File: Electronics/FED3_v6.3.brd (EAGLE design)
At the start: 108 x 50 mm, 50 parts, among them IC1 RTC_PCF8523T, IC2 TB6612 SSOP, IC3 M74VHC1GT50DTT1G, Q1 32.768, Q2 DMG3415, SW1 SSSS811101

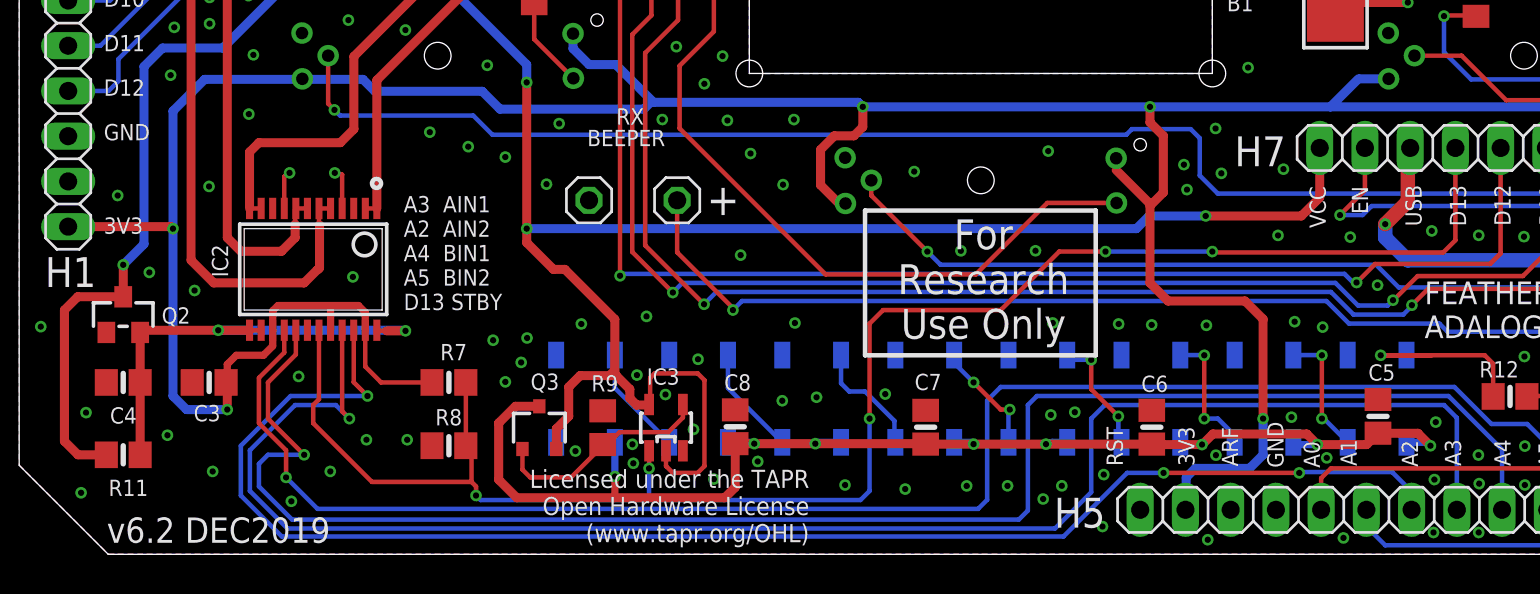
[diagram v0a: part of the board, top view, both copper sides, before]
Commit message: Added a secondary connector to plug the battery.
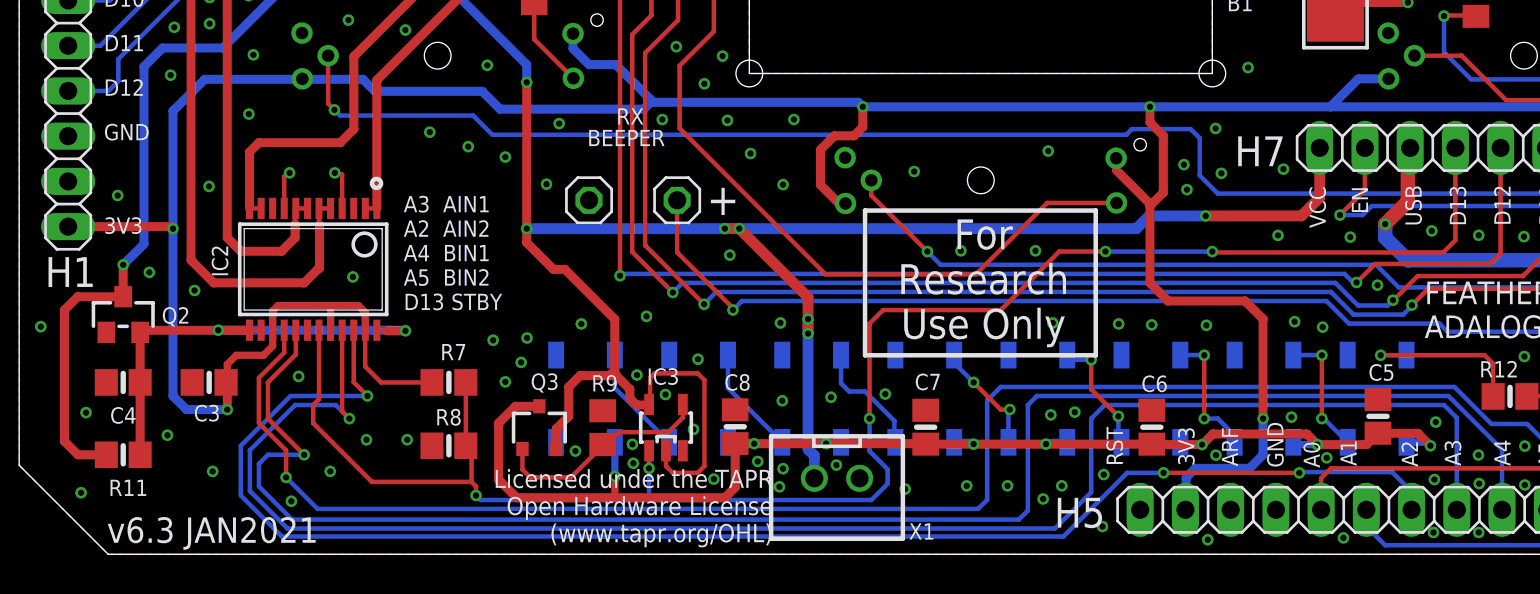
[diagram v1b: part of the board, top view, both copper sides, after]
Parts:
- added X1: B2B-PH-K-S(LF)(SN), Rembrandt Electronics - JST XH Connectors v1-0:JST-XH-02-PACKAGE-ROUND-PAD
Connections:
- net GND: now also X1.1
- net VCC: now also X1.2
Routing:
- net VCC: track 143.2 -> 160.6 mm, vias 4 -> 8
- net N$16: track 12.6 -> 9.82 mm
- net D13: track 97.2 -> 98.4 mm
- net VCCNEO: track 75.2 -> 74.4 mm
- net GND: vias 157 -> 159
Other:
- board text added: "v6.3 JAN2021"
- board text removed: "v6.2 DEC2019"
